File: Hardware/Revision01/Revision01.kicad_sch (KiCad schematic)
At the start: 26 parts, among them J1 Battery connector, SW1 Power-switch connection, SW2 SW_SPST_LED

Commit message: implemented feedback
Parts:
- removed SW1: Power-switch connection, symbol Connector_Generic:Conn_01x02
- removed TP10, TP11, TP16, TP7, TP8, TP9: TestPoint, TestPoint:TestPoint_THTPad_1.0x1.0mm_Drill0.5mm, symbol Connector:TestPoint
- added C46, C47: 10uF, Capacitor_SMD:C_1206_3216Metric, symbol Device:C
- added N1: Battery Holder, symbol Mechanical:Housing
- added U10: NCP1117LPST50T3G, NCP1117LPST50T3G:SOT230P700X180-4N, symbol NCP1117LPST50T3G:NCP1117LPST50T3G
- SW2: Distributor link (none) -> https://www.digikey.ca/en/products/detail/e-switch/200UDP1T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; Manufacturer Part Number (none) -> MP0045/1E2RD012
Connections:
- net +5V: now also C46.1, U10.2 (OUT)
- net BatteryV: now also SW2.1, SW2.3 (K), C47.1, U10.3 (IN)
- net GND: now also BT1.2 (-), BT2.2 (-), BT3.2 (-), BT4.2 (-), J1.2 (Pin_2), C46.2, C47.2, U10.1 (GND); no longer J1.1 (Pin_1)
- net at BT2.1 (+): now also BT1.1 (+), BT3.1 (+), BT4.1 (+), J1.1 (Pin_1), SW2.2, SW2.4 (A)
- no-connect marks 0 -> 24
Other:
- sheet Controller ports: added PA10/USART1_RX/TIM1_CH3, PA11/USART1_CTS/CANRX/USBDM/TIM1_CH4, PA12/USART1_RTS/CANTX/USBDP/TIM1_ETR, PA15/TIM2_CH1_ETR/SPI1_NSS, PA5_LED2/SPI1_SCK/ADC12_IN5, PA6/SPI1_MISO/ADC12_IN6/TIM3_CH1/TIM2_BKIN, PA7/SPI1_MOSI/ADC12_IN7/TIM3_CH2/TIM1_CH1N, PA8/USART1_CK/TIM1_CH1/MCO, PA9/USART1_TX/TIM1_CH2, PB10/I2C2_SCL/USART3_TX/TIM2_CH3, PB12/SPI2_NSS/I2C2_SMBAL/USART3_CK/TIM1_BKIN, PB1/ADC12_IN9/TIM3_CH4/TIM1_CH3N, PB4/TIM3_CH1/PB4/SPI1_MISO, PB5/I2C1_SMBAL/TIM3_CH2/SPI1_MOSI, PB6/TIM4_CH3/I2C1_SCL/CANRX, PB7/I2C1_SDA/TIM4_CH2/USART1_RX, PB8/TIM4_CH3/I2C1_SCL/CANRX, PB9/TIM4_CH4/I2C1_SDA/CANTX, PC10/USART3_TX, PC11/USART3_RX, PC12/USART3_CK, PC2/ADC12_IN12, PC3/ADC12_IN13, PC7/TIM3_CH2, PC9/TIM3_CH4, PD2/TIM3_ETR; removed +V_BATT, BOOT0, PB1, PC2, PC3, STLK_RX_USART2, STLK_TX_USART2, SWCLK, SWDIO, TRACESWO
- note added: "LDO: V_battery -> 5V -> Nucleo 5V Vin (-0.3 - 18V) 1A FLA Remove the power JP5 on nucleo board before using this daughterboard for receiving application"
- note removed: "+V_BATT is not an output"
- note removed: "Add this case switch & LED to BOM"
- note removed: "NEEDS TO FOLLOW PIN-Purpose Standard"
- note removed: "NEEDS TO FOLLOW PIN_Purpose Standard"
- note removed: "We need a battery symbol"
- note removed: "footprint added for nucleo board GOAL THIS WEEK - BEFORE FRIDAY HAVE EVERYTHING SETUP TO LAYOUT PCB Following this, complete layout of PCB on friday CREATE STM32CUBEIDE file to verify all ports Check over CONTROLLER SHEET To do before PCB LAYOUT MONDAY Improve annotation ordering Perform ERC check Move testpoints out of controller sheet TUESDAY Read and take notes on how to place COMPONENTS ON PC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"
- moved on the sheet: BT1, BT2, BT3, BT4, FID1, FID2, FID3, H1, H2, H3, H4, J1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

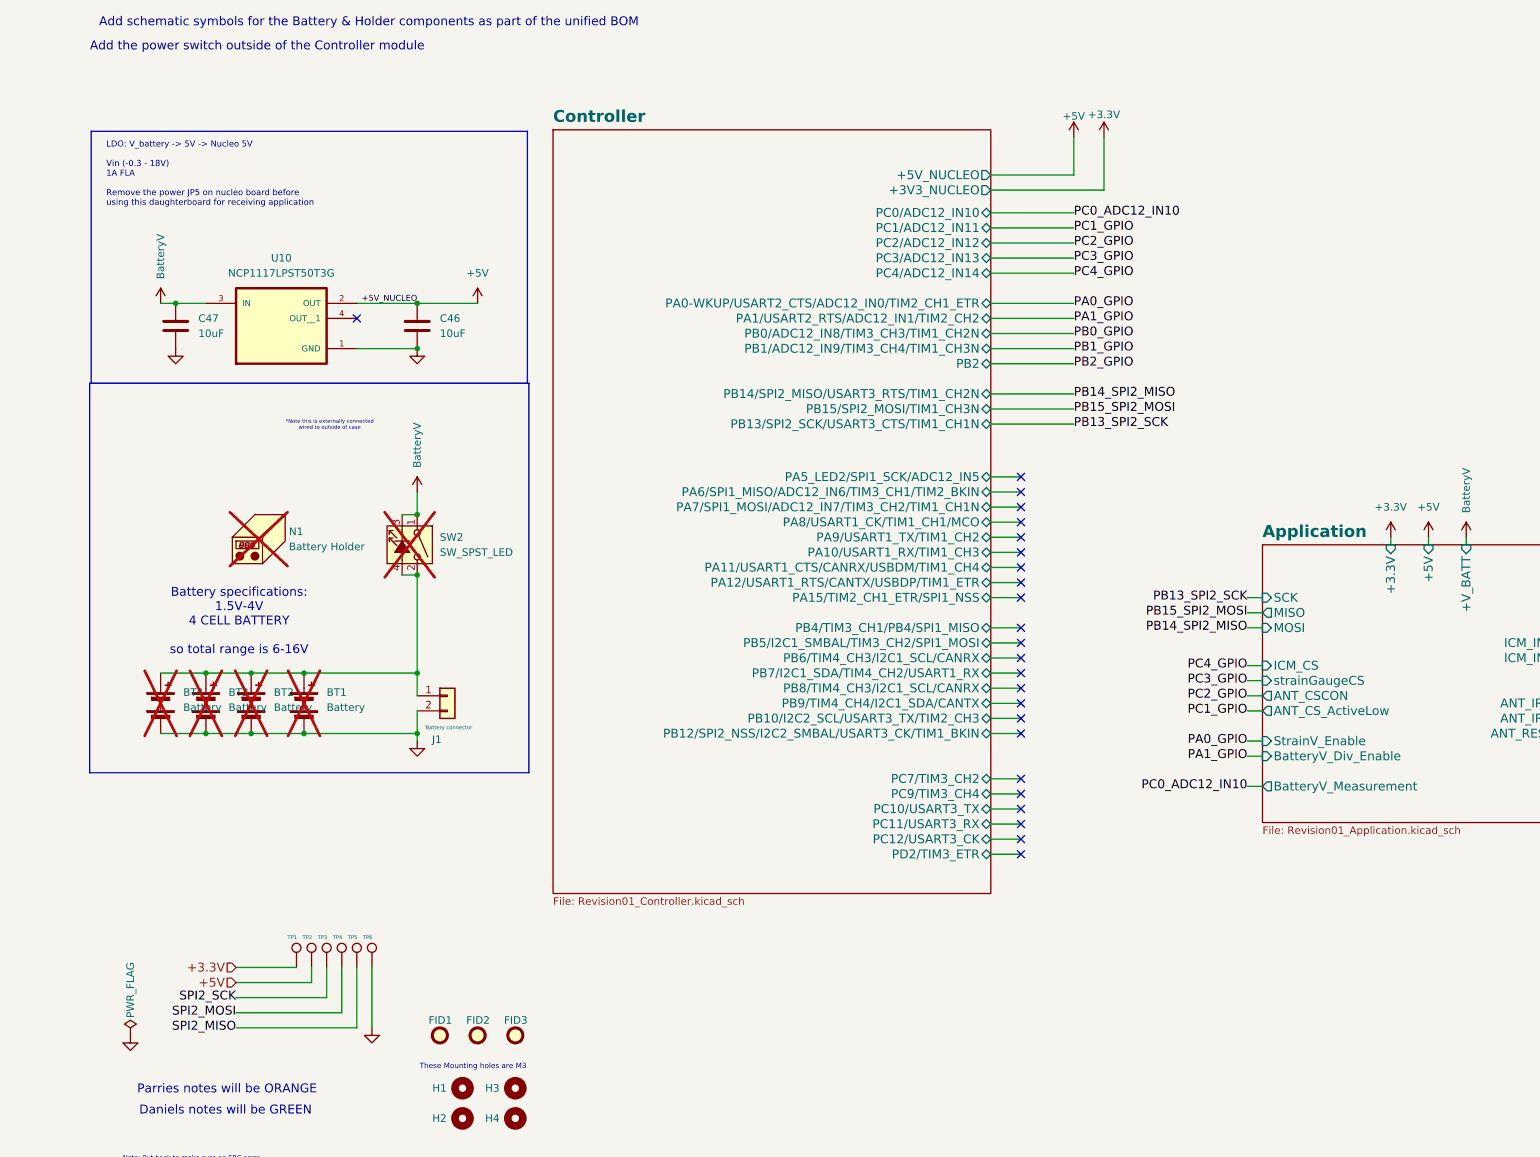
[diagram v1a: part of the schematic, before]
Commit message: some additional footprints assigned,
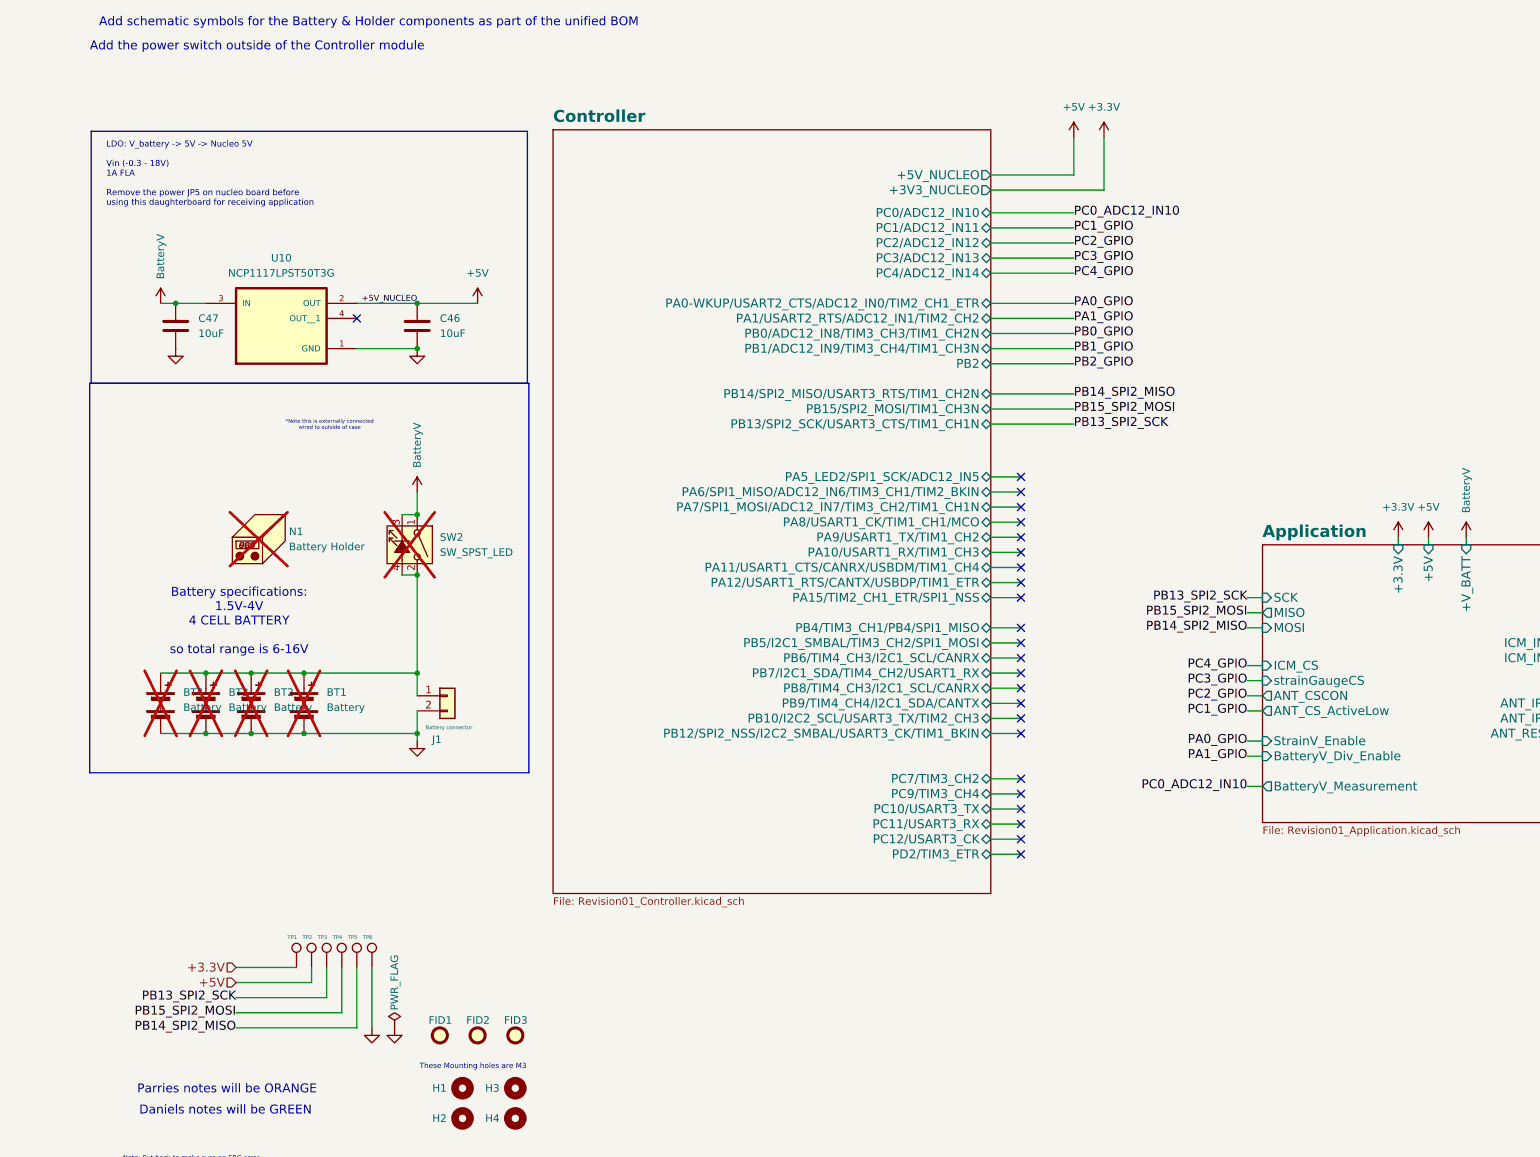
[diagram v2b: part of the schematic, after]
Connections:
- net SPI2_MISO is gone; now on net PB14_SPI2_MISO: TP5.1
- net SPI2_MOSI is gone; now on net PB15_SPI2_MOSI: TP4.1
- net SPI2_SCK is gone; now on net PB13_SPI2_SCK: TP3.1

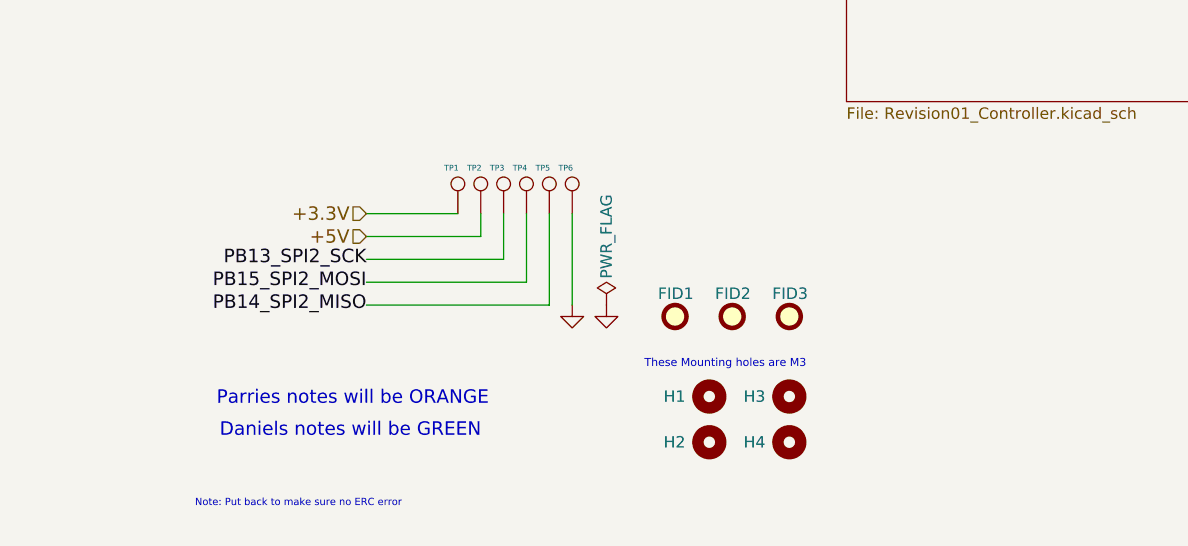
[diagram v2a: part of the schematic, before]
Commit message: added back powerflags back for ERC
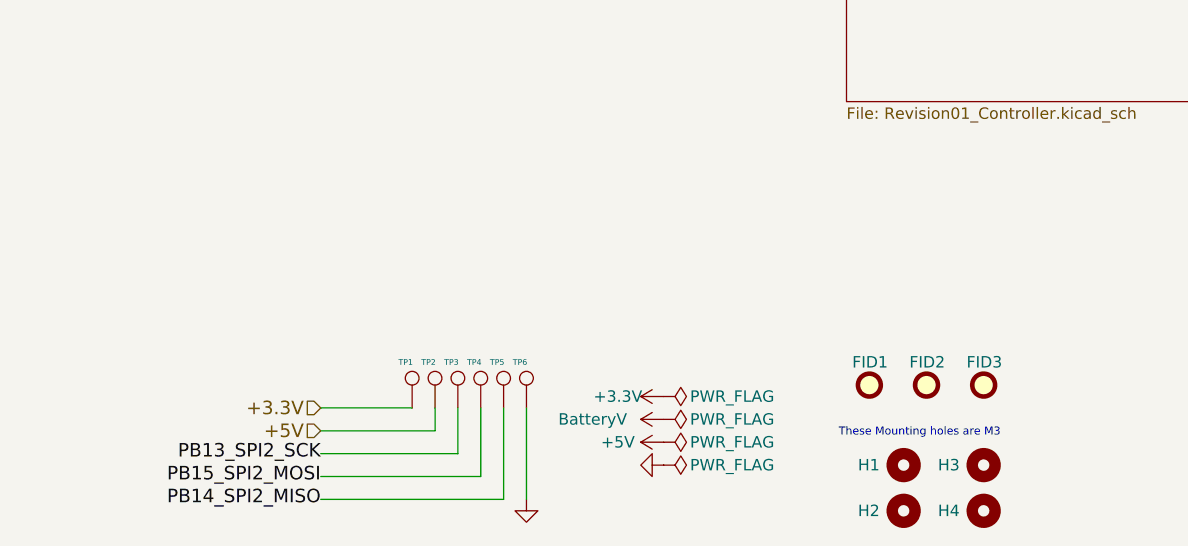
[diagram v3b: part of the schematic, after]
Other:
- note removed: "Daniels notes will be GREEN"
- note removed: "Note: Put back to make sure no ERC error"
- note removed: "Parries notes will be ORANGE"
- moved on the sheet: FID1, FID2, FID3, H1, H2, H3, H4, TP1, TP2, TP3, TP4, TP5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

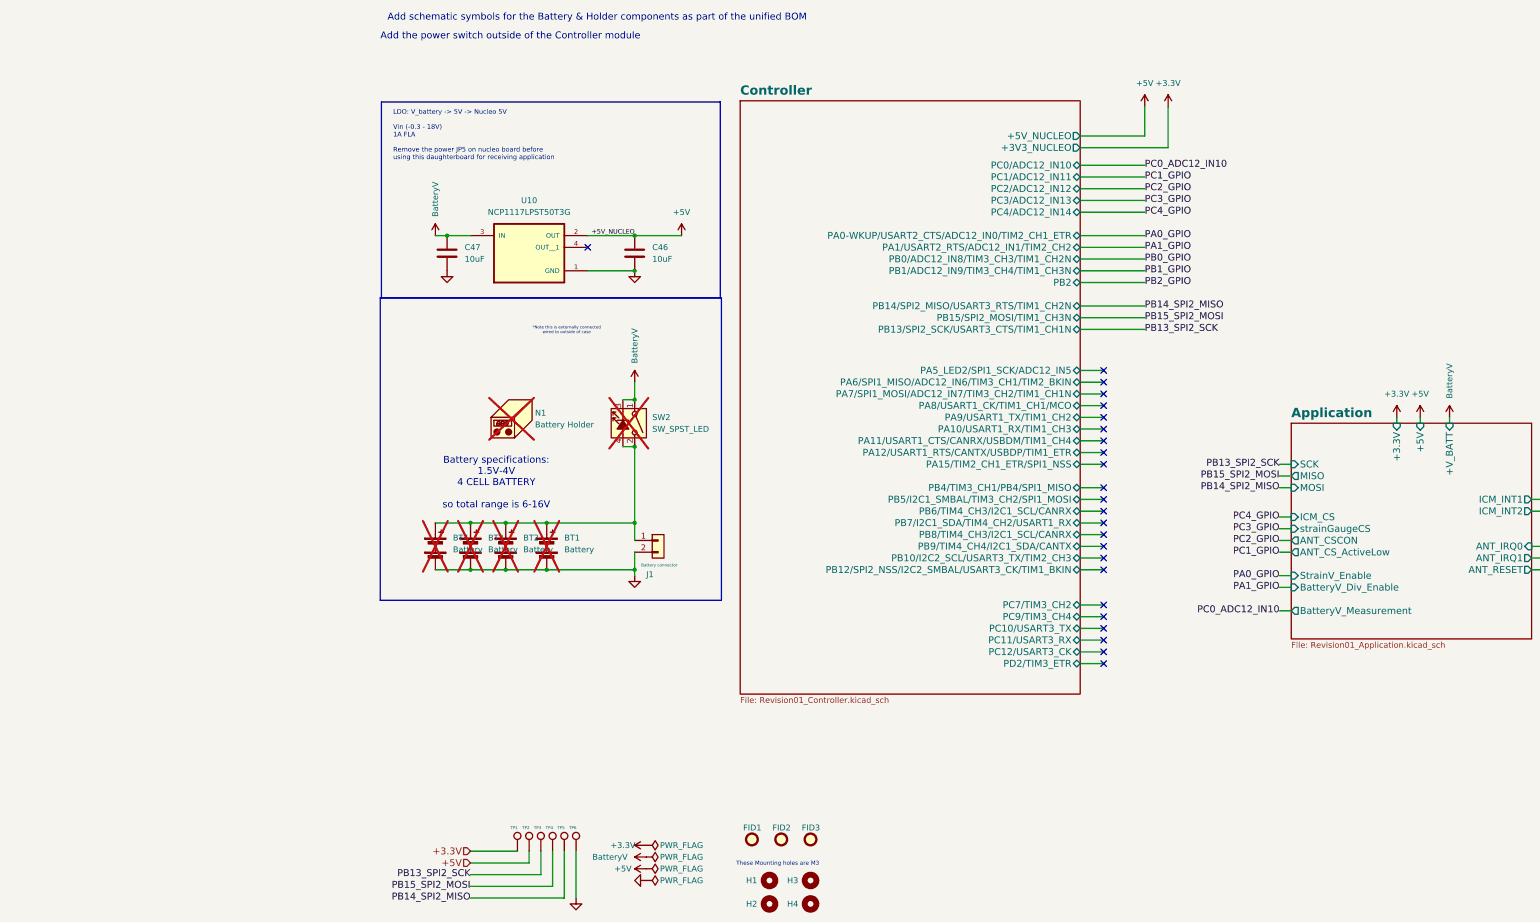
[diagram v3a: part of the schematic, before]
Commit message: added netclasses again changed power to be globally used strain gauges symbol created and added to schematic
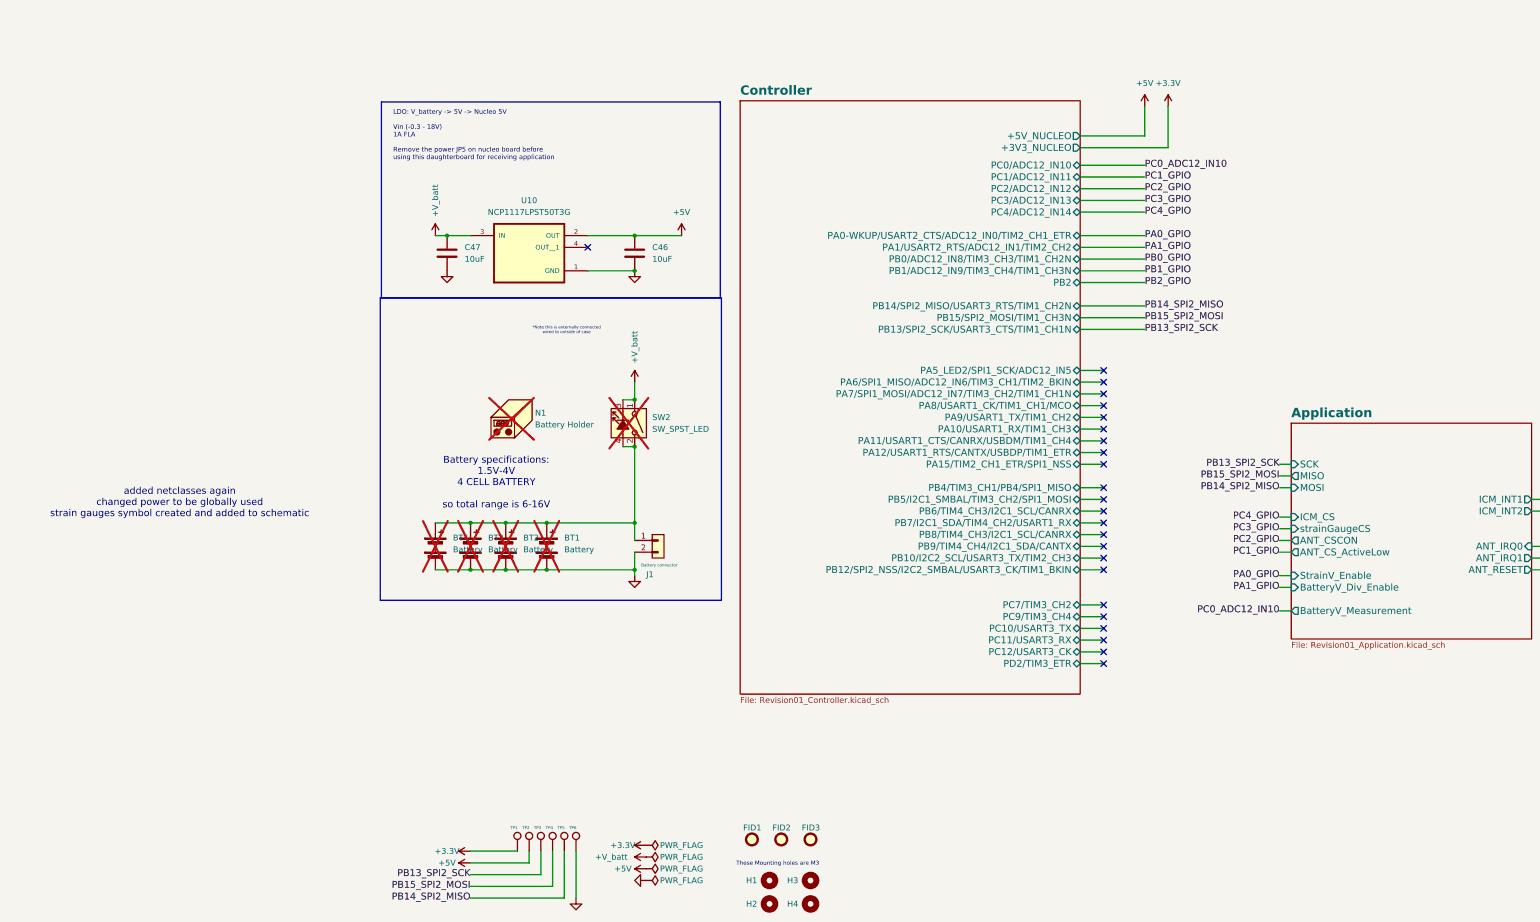
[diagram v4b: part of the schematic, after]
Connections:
- net BatteryV renamed +V_batt
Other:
- sheet Application ports: added none; removed +3.3V, +5V, +V_BATT
- note added: "added netclasses again changed power to be globally used strain gauges symbol created and added to schematic"
- note removed: "Add schematic symbols for the Battery & Holder components as part of the unified BOM"
- note removed: "Add the power switch outside of the Controller module"

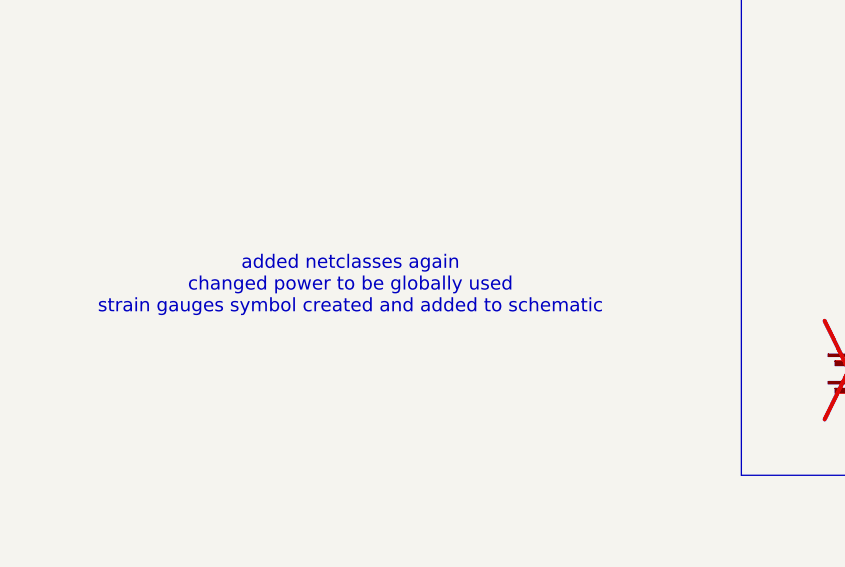
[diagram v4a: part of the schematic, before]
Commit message: added 0ohm resistor to power STRAIN GAUGE. Need to re-read ADC to ensure reference is able to read negative voltage, as well as is capable of reading strain gauge
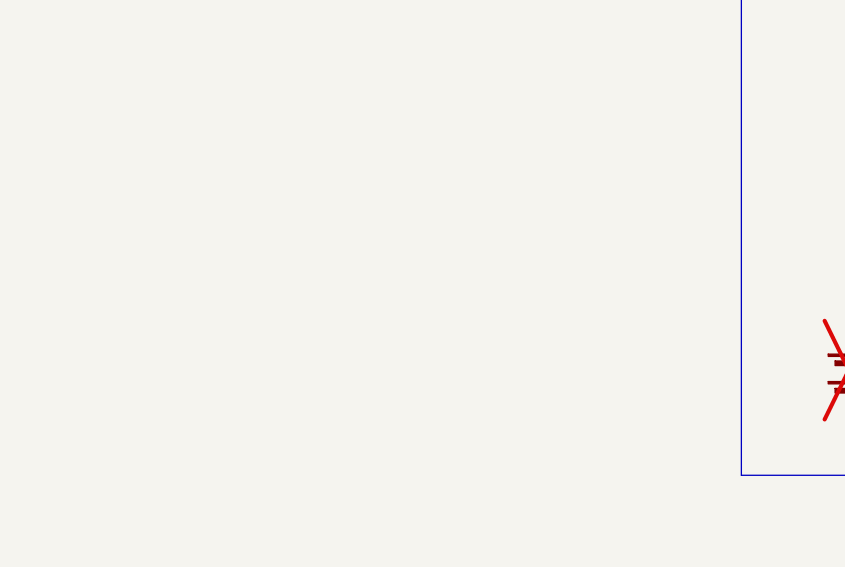
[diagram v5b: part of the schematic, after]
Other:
- note removed: "added netclasses again changed power to be globally used strain gauges symbol created and added to schematic"
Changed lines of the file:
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@@
-		)
-	)
-	(text "added netclasses again\nchanged power to be globally used\nstrain gauges symbol created and added to schematic"
-		(exclude_from_sim no)
-		(at -28.702 108.712 0)
-		(effects
-			(font
-				(size 1.4986 1.4986)
-			)
 		)
 	)

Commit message: added new battery measurement circuit which uses load switches onto schematic and changed headers to screw terminals
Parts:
- C46, C47: Manufacturer Part Number KGM21NR71E104KT -> CL31B106KAHNNNE
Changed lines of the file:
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@@
 			)
 		)
-		(property "Manufacturer Part Number" "KGM21NR71E104KT"
+		(property "Manufacturer Part Number" "CL31B106KAHNNNE"
 			(at 70.104 55.626 0)
 			(effects
@@
 			)
 		)
-		(property "Manufacturer Part Number" "KGM21NR71E104KT"
+		(property "Manufacturer Part Number" "CL31B106KAHNNNE"
 			(at 29.21 54.61 0)
 			(effects
